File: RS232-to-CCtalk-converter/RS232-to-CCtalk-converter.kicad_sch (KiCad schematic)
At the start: 23 parts, among them J1 DB9_Male, J2 Conn_01x04, J3 Conn_01x03, Q1 BC847, Q2 BC856A-QR, U1 ST232BDR, U2 UA78M05

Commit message: inital adding
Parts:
- removed C1, C2, C3, C4, C6: 1uF, Capacitor_SMD:C_0201_0603Metric, symbol Device:C_Small
- removed C5, C9: 100nF, Capacitor_SMD:C_0201_0603Metric, symbol Device:C_Small
- removed C7: 0.33uF, Capacitor_SMD:C_0201_0603Metric, symbol Device:C_Small
- removed C8: 10uF, Capacitor_SMD:C_0201_0603Metric, symbol Device:C_Small
- removed D1: BAT54J, Diode_SMD:D_SOD-323F, symbol Diode:BAT54J
- removed D2: BAT760, Diode_SMD:D_SOD-323F, symbol Diode:BAT54J
- removed J1: DB9_Male, Connector_Dsub:DSUB-9_Male_EdgeMount_P2.77mm, symbol Connector:DB9_Male
- removed J2: Conn_01x04, Connector:FanPinHeader_1x04_P2.54mm_Vertical, symbol Connector_Generic:Conn_01x04
- removed J3: Conn_01x03, Connector:FanPinHeader_1x03_P2.54mm_Vertical, symbol Connector_Generic:Conn_01x03
- removed Q1: BC847, Package_TO_SOT_SMD:SOT-23, symbol Transistor_BJT:BC847
- removed Q2: BC856A-QR, Package_TO_SOT_SMD:SOT-23, symbol Transistor_BJT:BC856
- removed R1, R3, R4: 10k, Resistor_SMD:R_0603_1608Metric, symbol Device:R_Small
- removed R2: 56R, Resistor_SMD:R_0603_1608Metric, symbol Device:R_Small
- removed R5: 100k, Resistor_SMD:R_0603_1608Metric, symbol Device:R_Small
- removed U1: ST232BDR, Package_SO:SOIC-16_4.55x10.3mm_P1.27mm, symbol Interface_UART:MAX232I
- removed U2: UA78M05, Package_TO_SOT_SMD:TO-252-3_TabPin2, symbol Regulator_Linear:L7805
- added C1, C2, C3, C4, C6: 1uF, RS232-to-CCtalk-converter-lib:C_0603_1608Metric, symbol RS232-to-CCtalk-converter-lib:C
- added C5, C9: 100nF, RS232-to-CCtalk-converter-lib:C_0603_1608Metric, symbol RS232-to-CCtalk-converter-lib:C
- added C7: 0.33uF, RS232-to-CCtalk-converter-lib:C_0603_1608Metric, symbol RS232-to-CCtalk-converter-lib:C
- added C8: 10uF, RS232-to-CCtalk-converter-lib:C_0603_1608Metric, symbol RS232-to-CCtalk-converter-lib:C
- added D1: BAT54J, RS232-to-CCtalk-converter-lib:D_SOD-323F, symbol RS232-to-CCtalk-converter-lib:BAT54J
- added D2: BAT760, RS232-to-CCtalk-converter-lib:D_SOD-323F, symbol RS232-to-CCtalk-converter-lib:BAT54J
- added J1: DB9_Male, RS232-to-CCtalk-converter-lib:DSUB-9_Male_EdgeMount_P2.77mm, symbol RS232-to-CCtalk-converter-lib:DB9_Male
- added J2: Conn_01x04, RS232-to-CCtalk-converter-lib:FanPinHeader_1x04_P2.54mm_Vertical, symbol RS232-to-CCtalk-converter-lib:Conn_01x04
- added J3: Conn_01x03, RS232-to-CCtalk-converter-lib:FanPinHeader_1x03_P2.54mm_Vertical, symbol RS232-to-CCtalk-converter-lib:Conn_01x03
- added Q1: BC847, RS232-to-CCtalk-converter-lib:SOT-23, symbol RS232-to-CCtalk-converter-lib:BC847
- added Q2: BC856, RS232-to-CCtalk-converter-lib:SOT-23, symbol RS232-to-CCtalk-converter-lib:BC856
- added R1, R3, R4: 10K, RS232-to-CCtalk-converter-lib:R_0603_1608Metric, symbol RS232-to-CCtalk-converter-lib:R
- added R2: 56R, RS232-to-CCtalk-converter-lib:R_0603_1608Metric, symbol RS232-to-CCtalk-converter-lib:R
- added R5: 100K, RS232-to-CCtalk-converter-lib:R_0603_1608Metric, symbol RS232-to-CCtalk-converter-lib:R
- added U1: ST232B, RS232-to-CCtalk-converter-lib:SOIC-16_4.55x10.3mm_P1.27mm, symbol RS232-to-CCtalk-converter-lib:ST232B
- added U2: L7805, RS232-to-CCtalk-converter-lib:TO-252-3_TabPin2, symbol RS232-to-CCtalk-converter-lib:L7805
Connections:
- net +24V: now also C7.1, D2.1 (K), U2.1 (IN)
- net +5V: now also C1.1, C4.1, C5.1, C8.1, C9.1, J2.1 (Pin_1), Q2.2 (E), R1.1, U1.16 (VCC), U2.3 (OUT)
- net CCTALK-DATA: now also D1.1 (K), J3.2 (Pin_2), R1.2, R2.2
- net GNDREF: now also C2.2, C4.2, C5.2, C7.2, C8.2, C9.2, J1.5, J2.4 (Pin_4), J3.3 (Pin_3), Q1.2 (E), R5.1, U1.15 (GND), U2.2 (GND)
- net RX: now also J2.2 (Pin_2), R3.1, U1.12 (R1OUT)
- net RXout: now also J1.3, U1.13 (R1IN)
- net TX: now also D1.2 (A), J2.3 (Pin_3), U1.11 (T1IN)
- net TXout: now also J1.2, U1.14 (T1OUT)
- new net: C6.1, U1.1 (C1+)
- new net: C6.2, U1.3 (C1-)
- new net: Q1.3 (C), R2.1
- new net: Q2.1 (B), R3.2
- new net: Q2.3 (C), R4.1
- new net: Q1.1 (B), R4.2, R5.2
- new net: C3.1, U1.4 (C2+)
- new net: C3.2, U1.5 (C2-)
- new net: C1.2, U1.2 (VS+)
- new net: C2.1, U1.6 (VS-)
- new net: D2.2 (A), J3.1 (Pin_1)

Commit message: first milestone
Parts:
- J3: value Conn_01x03 -> CCtalk Cable
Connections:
- net GNDREF: now also J3.1 (Pin_1); no longer J3.3 (Pin_3)
- net at D2.2 (A): now also J3.3 (Pin_3); no longer J3.1 (Pin_1)
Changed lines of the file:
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@@
     )
     (property "Value" "Conn_01x04" (id 1) (at 266.7 142.8749 0)
-      (effects (font (size 1.27 1.27)) (justify left))
+      (effects (font (size 1.27 1.27)) (justify left) hide)
     )
     (property "Footprint" "RS232-to-CCtalk-converter-lib:FanPinHeader_1x04_P2.54mm_Vertical" (id 2) (at 264.16 140.335 0)
@@
     (pin "1")
   )
-  (symbol (lib_id "RS232-to-CCtalk-converter-lib:Conn_01x03") (at 264.795 93.98 0) (unit 1)
-    (in_bom yes) (on_board yes) (fields_autoplaced)
-    (property "Reference" "J3" (id 0) (at 267.97 92.7099 0)
-      (effects (font (size 1.27 1.27)) (justify left))
-    )
-    (property "Value" "Conn_01x03" (id 1) (at 267.97 95.2499 0)
-      (effects (font (size 1.27 1.27)) (justify left))
+  (symbol (lib_id "RS232-to-CCtalk-converter-lib:Conn_01x03") (at 264.795 93.98 0) (mirror x) (unit 1)
+    (in_bom yes) (on_board yes)
+    (property "Reference" "J3" (id 0) (at 267.335 93.345 0))
+    (property "Value" "CCtalk Cable" (id 1) (at 273.05 95.885 0)
+      (effects (font (size 1.27 1.27)) hide)
     )
     (property "Footprint" "RS232-to-CCtalk-converter-lib:FanPinHeader_1x03_P2.54mm_Vertical" (id 2) (at 264.795 93.98 0)
@@
     )
     (path "/f1cc83a0-6b19-46fb-8328-3a657b6e1e7d"
-      (reference "J3") (unit 1) (value "Conn_01x03") (footprint "RS232-to-CCtalk-converter-lib:FanPinHeader_1x03_P2.54mm_Vertical")
+      (reference "J3") (unit 1) (value "CCtalk Cable") (footprint "RS232-to-CCtalk-converter-lib:FanPinHeader_1x03_P2.54mm_Vertical")
     )
     (path "/cce57939-2ab1-4897-bc4c-99f3f0b3e064"

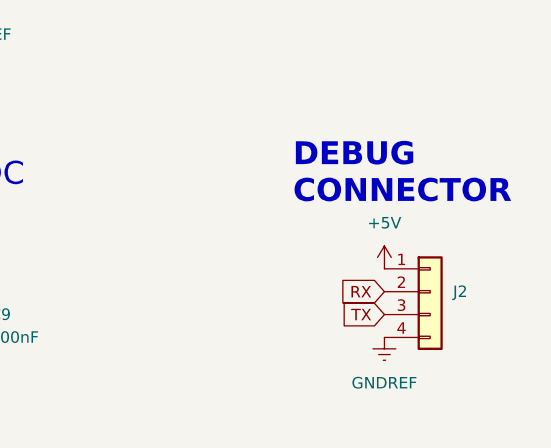
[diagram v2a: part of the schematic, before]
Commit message: add +5v to debug connector
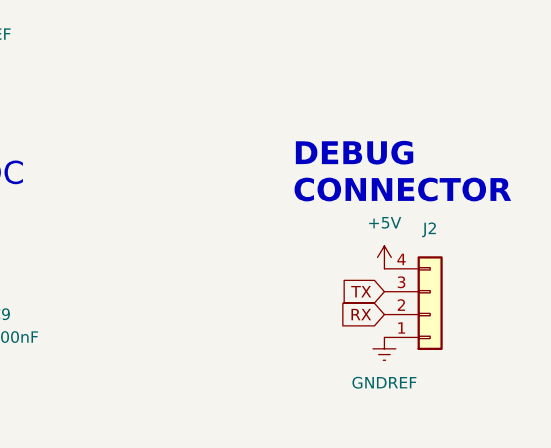
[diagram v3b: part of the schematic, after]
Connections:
- net +5V: now also J2.4 (Pin_4); no longer J2.1 (Pin_1)
- net GNDREF: now also J2.1 (Pin_1); no longer J2.4 (Pin_4)
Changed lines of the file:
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@@
     (effects (font (size 2.54 2.54) (thickness 0.508) bold) (justify left bottom))
   )
-  (global_label "TX" (shape input) (at 259.08 142.875 180) (fields_autoplaced)
-    (effects (font (size 1.27 1.27)) (justify right))
-    (property "Intersheet References" "${INTERSHEET_REFS}" (id 0) (at 254.4898 142.9544 0)
+  (global_label "TX" (shape input) (at 259.08 140.335 180) (fields_autoplaced)
+    (effects (font (size 1.27 1.27)) (justify right))
+    (property "Intersheet References" "${INTERSHEET_REFS}" (id 0) (at 254.4898 140.4144 0)
       (effects (font (size 1.27 1.27)) (justify right) hide)
     )
@@
     )
   )
-  (global_label "RX" (shape input) (at 259.08 140.335 180) (fields_autoplaced)
-    (effects (font (size 1.27 1.27)) (justify right))
-    (property "Intersheet References" "${INTERSHEET_REFS}" (id 0) (at 254.1874 140.4144 0)
+  (global_label "RX" (shape input) (at 259.08 142.875 180) (fields_autoplaced)
+    (effects (font (size 1.27 1.27)) (justify right))
+    (property "Intersheet References" "${INTERSHEET_REFS}" (id 0) (at 254.1874 142.9544 0)
       (effects (font (size 1.27 1.27)) (justify right) hide)
     )
@@
     (pin "1")
   )
-  (symbol (lib_id "RS232-to-CCtalk-converter-lib:Conn_01x04") (at 264.16 140.335 0) (unit 1)
-    (in_bom yes) (on_board yes) (fields_autoplaced)
-    (property "Reference" "J2" (id 0) (at 266.7 140.3349 0)
-      (effects (font (size 1.27 1.27)) (justify left))
-    )
-    (property "Value" "Conn_01x04" (id 1) (at 266.7 142.8749 0)
+  (symbol (lib_id "RS232-to-CCtalk-converter-lib:Conn_01x04") (at 264.16 142.875 0) (mirror x) (unit 1)
+    (in_bom yes) (on_board yes) (fields_autoplaced)
+    (property "Reference" "J2" (id 0) (at 264.16 133.35 0))
+    (property "Value" "Conn_01x04" (id 1) (at 266.7 140.3351 0)
       (effects (font (size 1.27 1.27)) (justify left) hide)
     )
-    (property "Footprint" "RS232-to-CCtalk-converter-lib:FanPinHeader_1x04_P2.54mm_Vertical" (id 2) (at 264.16 140.335 0)
-      (effects (font (size 1.27 1.27)) hide)
-    )
-    (property "Datasheet" "~" (id 3) (at 264.16 140.335 0)
-      (effects (font (size 1.27 1.27)) hide)
-    )
+    (property "Footprint" "RS232-to-CCtalk-converter-lib:FanPinHeader_1x04_P2.54mm_Vertical" (id 2) (at 264.16 142.875 0)
+      (effects (font (size 1.27 1.27)) hide)
+    )
+    (property "Datasheet" "~" (id 3) (at 264.16 142.875 0)
+      (effects (font (size 1.27 1.27)) hide)
+    )

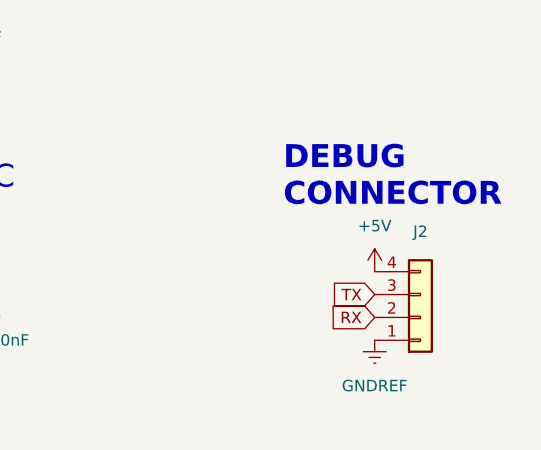
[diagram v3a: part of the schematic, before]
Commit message: remove +5V on debug connector
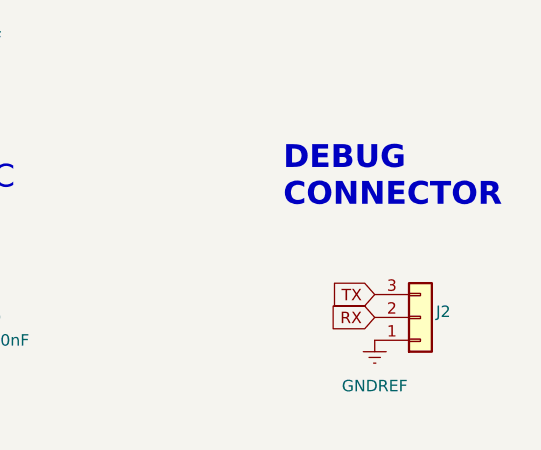
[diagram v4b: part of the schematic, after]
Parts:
- removed J2: Conn_01x04, RS232-to-CCtalk-converter-lib:FanPinHeader_1x04_P2.54mm_Vertical, symbol RS232-to-CCtalk-converter-lib:Conn_01x04
- added J2: CCtalk Cable, RS232-to-CCtalk-converter-lib:Header_1x03_P2.54mm_Vertical, symbol RS232-to-CCtalk-converter-lib:Conn_01x03
- J3: footprint RS232-to-CCtalk-converter-lib:FanPinHeader_1x03_P2.54mm_Vertical -> RS232-to-CCtalk-converter-lib:Header_1x03_P2.54mm_Vertical_with_holder
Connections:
- net GNDREF: now also J2.1 (Pin_1)
- net RX: now also J2.2 (Pin_2)
- net TX: now also J2.3 (Pin_3)
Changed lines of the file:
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@@
     (pin "2")
-  )
-  (symbol (lib_id "power:+5V") (at 259.08 137.795 0) (unit 1)
-    (in_bom yes) (on_board yes) (fields_autoplaced)
-    (property "Reference" "#PWR0115" (id 0) (at 259.08 141.605 0)
-      (effects (font (size 1.27 1.27)) hide)
-    )
-    (property "Value" "+5V" (id 1) (at 259.08 132.715 0))
-    (property "Footprint" "" (id 2) (at 259.08 137.795 0)
-      (effects (font (size 1.27 1.27)) hide)
-    )
-    (property "Datasheet" "" (id 3) (at 259.08 137.795 0)
-      (effects (font (size 1.27 1.27)) hide)
-    )
-    (pin "1")
   )
   (symbol (lib_id "power:GNDREF") (at 107.95 120.65 0) (unit 1)
@@
     (pin "1")
   )
-  (symbol (lib_id "RS232-to-CCtalk-converter-lib:Conn_01x04") (at 264.16 142.875 0) (mirror x) (unit 1)
-    (in_bom yes) (on_board yes) (fields_autoplaced)
-    (property "Reference" "J2" (id 0) (at 264.16 133.35 0))
-    (property "Value" "Conn_01x04" (id 1) (at 266.7 140.3351 0)
-      (effects (font (size 1.27 1.27)) (justify left) hide)
-    )
-    (property "Footprint" "RS232-to-CCtalk-converter-lib:FanPinHeader_1x04_P2.54mm_Vertical" (id 2) (at 264.16 142.875 0)
-      (effects (font (size 1.27 1.27)) hide)
-    )
-    (property "Datasheet" "~" (id 3) (at 264.16 142.875 0)
-      (effects (font (size 1.27 1.27)) hide)
-    )
-    (pin "1")
-    (pin "2")
-    (pin "3")
-    (pin "4")
-  )
   (symbol (lib_id "RS232-to-CCtalk-converter-lib:BC856") (at 211.455 80.01 0) (mirror x) (unit 1)
     (in_bom yes) (on_board yes) (fields_autoplaced)
@@
     )
     (property "MPN" "BC847CWT1G" (id 4) (at 203.835 95.25 0)
+      (effects (font (size 1.27 1.27)) hide)
+    )
+    (pin "1")
+    (pin "2")
+    (pin "3")
+  )
+  (symbol (lib_id "RS232-to-CCtalk-converter-lib:Conn_01x03") (at 264.16 142.875 0) (mirror x) (unit 1)
+    (in_bom yes) (on_board yes)
+    (property "Reference" "J2" (id 0) (at 266.7 142.24 0))
+    (property "Value" "CCtalk Cable" (id 1) (at 272.415 144.78 0)
+      (effects (font (size 1.27 1.27)) hide)
+    )
+    (property "Footprint" "RS232-to-CCtalk-converter-lib:Header_1x03_P2.54mm_Vertical" (id 2) (at 264.16 142.875 0)
+      (effects (font (size 1.27 1.27)) hide)
+    )
+    (property "Datasheet" "~" (id 3) (at 264.16 142.875 0)
       (effects (font (size 1.27 1.27)) hide)
     )
@@
       (effects (font (size 1.27 1.27)) hide)
     )
-    (property "Footprint" "RS232-to-CCtalk-converter-lib:FanPinHeader_1x03_P2.54mm_Vertical" (id 2) (at 264.795 93.98 0)
+    (property "Footprint" "RS232-to-CCtalk-converter-lib:Header_1x03_P2.54mm_Vertical_with_holder" (id 2) (at 264.795 93.98 0)
       (effects (font (size 1.27 1.27)) hide)
     )
@@
       (reference "#PWR0114") (unit 1) (value "GNDREF") (footprint "")
     )
-    (path "/0a688352-8717-42f8-adb2-65b5b5c39458"
-      (reference "#PWR0115") (unit 1) (value "+5V") (footprint "")
-    )
     (path "/4f2b7598-0a44-4566-b937-1a484bc3080c"
       (reference "#PWR0116") (unit 1) (value "GNDREF") (footprint "")
@@
       (reference "J1") (unit 1) (value "DB9_Male") (footprint "RS232-to-CCtalk-converter-lib:DSUB-9_Male_EdgeMount_P2.77mm")
     )
-    (path "/b506915e-9542-4b8e-a765-4557701981de"
-      (reference "J2") (unit 1) (value "Conn_01x04") (footprint "RS232-to-CCtalk-converter-lib:FanPinHeader_1x04_P2.54mm_Vertical")
+    (path "/cee2ca0f-9764-42dd-9fd2-6700a2d8efae"
+      (reference "J2") (unit 1) (value "CCtalk Cable") (footprint "RS232-to-CCtalk-converter-lib:Header_1x03_P2.54mm_Vertical")
     )
     (path "/f1cc83a0-6b19-46fb-8328-3a657b6e1e7d"
-      (reference "J3") (unit 1) (value "CCtalk Cable") (footprint "RS232-to-CCtalk-converter-lib:FanPinHeader_1x03_P2.54mm_Vertical")
+      (reference "J3") (unit 1) (value "CCtalk Cable") (footprint "RS232-to-CCtalk-converter-lib:Header_1x03_P2.54mm_Vertical_with_holder")
     )
     (path "/cce57939-2ab1-4897-bc4c-99f3f0b3e064"

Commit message: generate BOM, drills and gerbers
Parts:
- removed J1: DB9_Male, RS232-to-CCtalk-converter-lib:DSUB-9_Male_EdgeMount_P2.77mm, symbol RS232-to-CCtalk-converter-lib:DB9_Male
- added J1: DB9_Female, RS232-to-CCtalk-converter-lib:DSUB-9_Male_EdgeMount_P2.77mm, symbol Connector:DB9_Female
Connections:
- net GNDREF: now also J1.5
- net RXout: now also J1.3
- net TXout: now also J1.2
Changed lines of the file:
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@@
     (pin "2")
-  )
-  (symbol (lib_id "RS232-to-CCtalk-converter-lib:DB9_Male") (at 36.195 91.44 0) (mirror y) (unit 1)
-    (in_bom yes) (on_board yes) (fields_autoplaced)
-    (property "Reference" "J1" (id 0) (at 36.195 72.39 0))
-    (property "Value" "DB9_Male" (id 1) (at 36.195 74.93 0))
-    (property "Footprint" "RS232-to-CCtalk-converter-lib:DSUB-9_Male_EdgeMount_P2.77mm" (id 2) (at 36.195 91.44 0)
-      (effects (font (size 1.27 1.27)) hide)
-    )
-    (property "Datasheet" " ~" (id 3) (at 36.195 91.44 0)
-      (effects (font (size 1.27 1.27)) hide)
-    )
-    (pin "1")
-    (pin "2")
-    (pin "3")
-    (pin "4")
-    (pin "5")
-    (pin "6")
-    (pin "7")
-    (pin "8")
-    (pin "9")
   )
   (symbol (lib_id "power:+24V") (at 175.26 137.795 0) (unit 1)
@@
     (pin "2")
   )
+  (symbol (lib_id "Connector:DB9_Female") (at 36.195 91.44 180) (unit 1)
+    (in_bom yes) (on_board yes)
+    (property "Reference" "J1" (id 0) (at 36.195 78.105 0))
+    (property "Value" "DB9_Female" (id 1) (at 36.195 75.565 0)
+      (effects (font (size 1.27 1.27)) hide)
+    )
+    (property "Footprint" "RS232-to-CCtalk-converter-lib:DSUB-9_Male_EdgeMount_P2.77mm" (id 2) (at 36.195 91.44 0)
+      (effects (font (size 1.27 1.27)) hide)
+    )
+    (property "Datasheet" "https://hr.mouser.com/datasheet/2/296/999-YYY-E30SY02-1539073.pdf" (id 3) (at 36.195 91.44 0)
+      (effects (font (size 1.27 1.27)) hide)
+    )
+    (property "MPN" "MHDTZK9-DB9S-K" (id 4) (at 36.195 91.44 0)
+      (effects (font (size 1.27 1.27)) hide)
+    )
+    (pin "1")
+    (pin "2")
+    (pin "3")
+    (pin "4")
+    (pin "5")
+    (pin "6")
+    (pin "7")
+    (pin "8")
+    (pin "9")
+  )
   (symbol (lib_id "RS232-to-CCtalk-converter-lib:BAT54J") (at 259.715 86.36 270) (unit 1)
     (in_bom yes) (on_board yes) (fields_autoplaced)
@@
       (reference "D2") (unit 1) (value "BAT760") (footprint "RS232-to-CCtalk-converter-lib:D_SOD-323F")
     )
-    (path "/9ce175c8-c768-471d-9f86-e6146ae09f72"
-      (reference "J1") (unit 1) (value "DB9_Male") (footprint "RS232-to-CCtalk-converter-lib:DSUB-9_Male_EdgeMount_P2.77mm")
+    (path "/e37daa04-b262-4f7e-8ef7-14142bb24e98"
+      (reference "J1") (unit 1) (value "DB9_Female") (footprint "RS232-to-CCtalk-converter-lib:DSUB-9_Male_EdgeMount_P2.77mm")
     )
     (path "/cee2ca0f-9764-42dd-9fd2-6700a2d8efae"

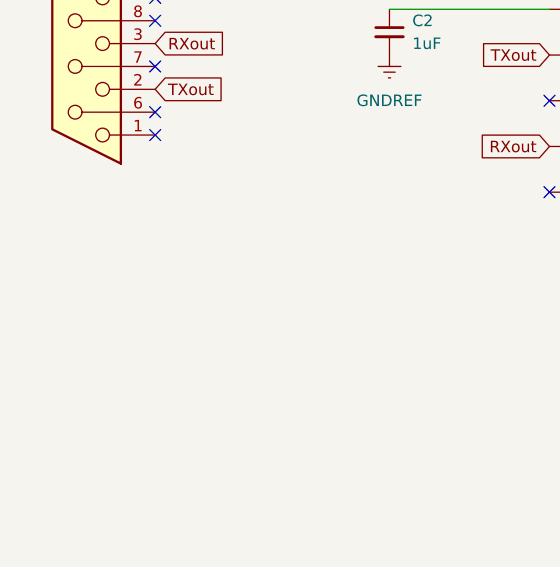
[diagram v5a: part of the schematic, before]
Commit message: replace 3d model db9; add new mpn db9; generate new outputs
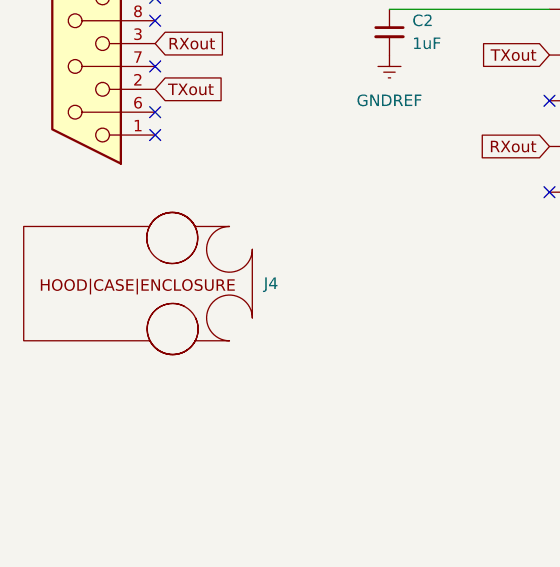
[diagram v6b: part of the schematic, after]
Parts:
- added J4: DB9_female_hood, RS232-to-CCtalk-converter-lib:DSUB-9_Female_wire_mount_P2.77mm_hood, symbol RS232-to-CCtalk-converter-lib:DB9_female_hood
- J1: MPN MHDTZK9-DB9S-K -> DE09S064TLF
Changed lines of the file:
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@@
       (effects (font (size 1.27 1.27)) hide)
     )
-    (property "MPN" "MHDTZK9-DB9S-K" (id 4) (at 36.195 91.44 0)
+    (property "MPN" "DE09S064TLF" (id 4) (at 36.195 91.44 0)
       (effects (font (size 1.27 1.27)) hide)
     )
@@
     (pin "3")
   )
+  (symbol (lib_id "RS232-to-CCtalk-converter-lib:DB9_female_hood") (at 39.37 121.92 0) (unit 1)
+    (in_bom yes) (on_board yes) (fields_autoplaced)
+    (property "Reference" "J4" (id 0) (at 55.88 118.1099 0)
+      (effects (font (size 1.27 1.27)) (justify left))
+    )
+    (property "Value" "DB9_female_hood" (id 1) (at 39.37 109.22 0)
+      (effects (font (size 1.27 1.27)) hide)
+    )
+    (property "Footprint" "RS232-to-CCtalk-converter-lib:DSUB-9_Female_wire_mount_P2.77mm_hood" (id 2) (at 39.37 121.92 0)
+      (effects (font (size 1.27 1.27)) hide)
+    )
+    (property "Datasheet" "https://www.mouser.com/catalog/specsheets/bel_cnch-s-a0001292862-1.pdf?_gl=1*j6ag6q*_gcl_aw*R0NMLjE3Mzg2MjExOTguQ2p3S0NBaUE3NEc5QmhBRUVpd0E4a05mcGFMSHVERURYMTJFLTN5OFRpdmtUN2k5VWd2aGFIcERzYWxuM3RPRXJJeWROYXUtRFdsSUpSb0NMcklRQXZEX0J3RQ..*_gcl_au*MTM4NjE2MDYwNy4xNzM3NjQ1NTQ4*_ga*MjAyNDU4Mjg5NC4xNzQwMzI5MDEw*_ga_15W4STQT4T*MTc0MDMyOTAxMC4xLjEuMTc0MDMyOTk3OS4yMS4wLjA." (id 3) (at 39.37 121.92 0)
+      (effects (font (size 1.27 1.27)) hide)
+    )
+    (property "MPN" "40-9709H" (id 4) (at 39.37 121.92 0)
+      (effects (font (size 1.27 1.27)) hide)
+    )
+  )
   (symbol (lib_id "RS232-to-CCtalk-converter-lib:C") (at 212.09 144.145 0) (unit 1)
     (in_bom yes) (on_board yes) (fields_autoplaced)
@@
       (reference "J3") (unit 1) (value "CCtalk Cable") (footprint "RS232-to-CCtalk-converter-lib:Header_1x03_P2.54mm_Vertical_with_holder")
     )
+    (path "/fdca5397-21f8-49f8-89d5-c95848bfeae5"
+      (reference "J4") (unit 1) (value "DB9_female_hood") (footprint "RS232-to-CCtalk-converter-lib:DSUB-9_Female_wire_mount_P2.77mm_hood")
+    )
     (path "/cce57939-2ab1-4897-bc4c-99f3f0b3e064"
